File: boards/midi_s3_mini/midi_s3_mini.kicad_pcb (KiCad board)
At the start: 2 copper layers, 90 x 70 mm, 35 parts, among them J1 Power2, J10 PLAY_CUE, J11 JOG, J12 TEMPO, J2 Power1, J3 UART_PI, J4 1BTN_A_TX, J5 1BTN_A_RX, J6 1BTN_B_RX, J7 1BTN_B_TX, J8 LOOP, J9 TRACK_ENC, U1 LOLIN_S3_Mini

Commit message: Design the new power supply system
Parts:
- removed C1, C10, C11, C12, C13, C3, C4, C7, C8, C9: 100n, easyeda2kicad:CAP-TH_L4.2-W3.5-P2.54-D0.5
- removed C2: 1000uF / 35 V, easyeda2kicad:CAP-TH_BD10.0-P5.00-D1.0-FD
- removed C5: 10u / 50 V, easyeda2kicad:CAP-TH_BD5.0-P2.00-D0.8-FD
- removed C6: 22u 50V, easyeda2kicad:CAP-TH_BD5.0-P2.00-D0.5-FD
- removed R1, R3: 1.8k, easyeda2kicad:RES-TH_BD2.4-L6.3-P10.30-D0.6
- removed R2, R4: 3.3k, easyeda2kicad:RES-TH_BD2.2-L6.5-P10.50-D0.6
- removed R5: 10k, easyeda2kicad:RES-TH_BD2.5-L6.5-P10.50-D0.6
- moved J11 75.4 mm to (84.9, 85.6), turned to 180 degrees
- moved J12 74.5 mm to (99.6, 85.7), turned to 0 degrees
- moved J8 74.5 mm to (33.7, 85.8), turned to 0 degrees
- moved J3 70.9 mm to (22.2, 56.9), turned to -90 degrees
- moved U1 35.1 mm to (47.9, 24.3), turned to 0 degrees
- moved J1 13.5 mm to (23.4, 44.7)
- moved J2 13.5 mm to (23.4, 35.0)
- moved J10 7.75 mm to (52.4, 85.7)
- moved J9 1.77 mm to (69.2, 85.6)
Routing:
- net +5V: track 193.9 -> 0.00 mm, vias 2 -> 0
- net +3.3V: track 58.4 -> 0.00 mm, vias 3 -> 0
- net /1BTNA_TX: track 52.5 -> 0.00 mm, vias 1 -> 0
- net /1BTNB_TX: track 45.6 -> 0.00 mm, vias 1 -> 0
- net /JOG1: track 44.6 -> 0.00 mm
- net /1BTNA_RX: track 40.3 -> 0.00 mm, vias 1 -> 0
- net /JOG2: track 39.0 -> 0.00 mm
- net /1BTNB_RX: track 35.2 -> 0.00 mm, vias 1 -> 0
- net /UART_RX_FROM_PI: track 33.5 -> 0.00 mm
- net /BTN_PLAY: track 31.8 -> 0.00 mm
- net /LOOP_END_BTN: track 30.2 -> 0.00 mm, vias 1 -> 0
- net /LED_CUE: track 28.8 -> 0.00 mm
- net /BTN_CUE: track 28.6 -> 0.00 mm
- net /LED_PLAY: track 28.4 -> 0.00 mm
- net /ENC_SW: track 27.3 -> 0.00 mm
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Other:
- board text added: "vvv USB-C side vvv"

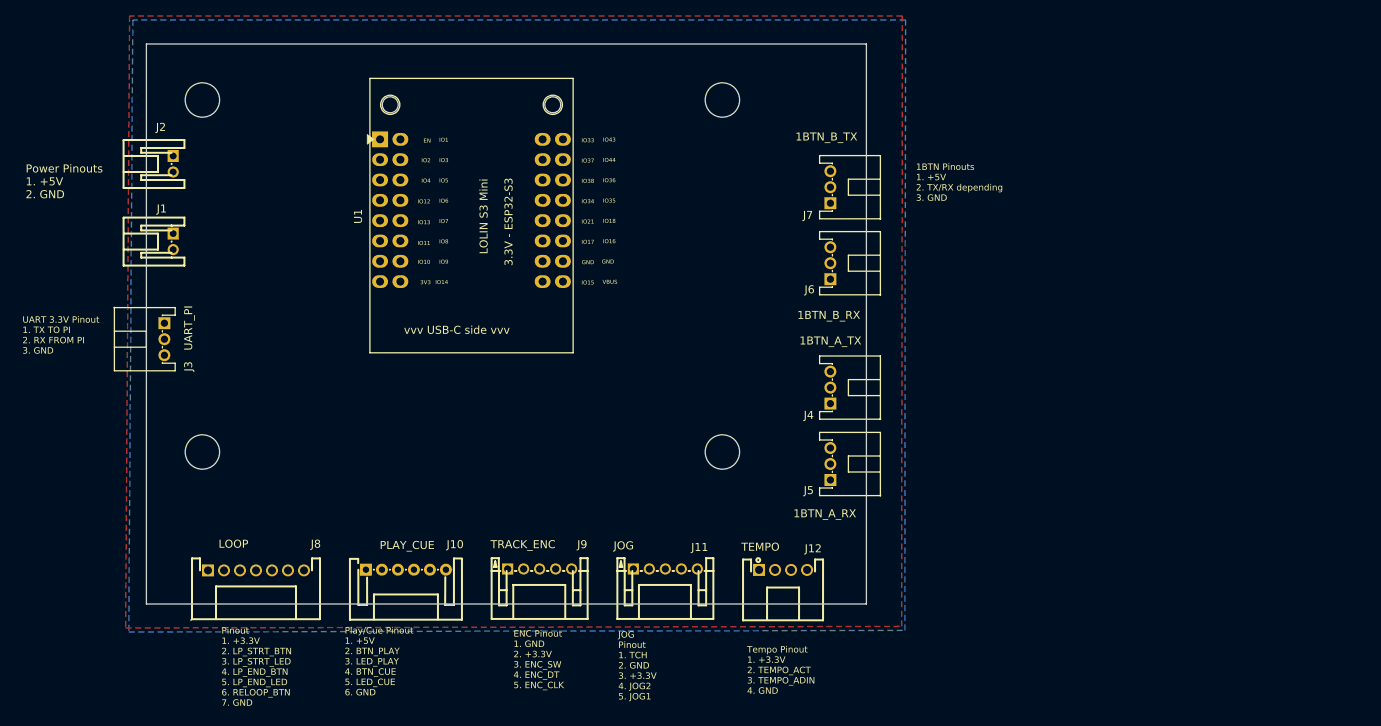
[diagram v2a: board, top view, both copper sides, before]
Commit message: Finish the ESD and power system for the V2 midi S3
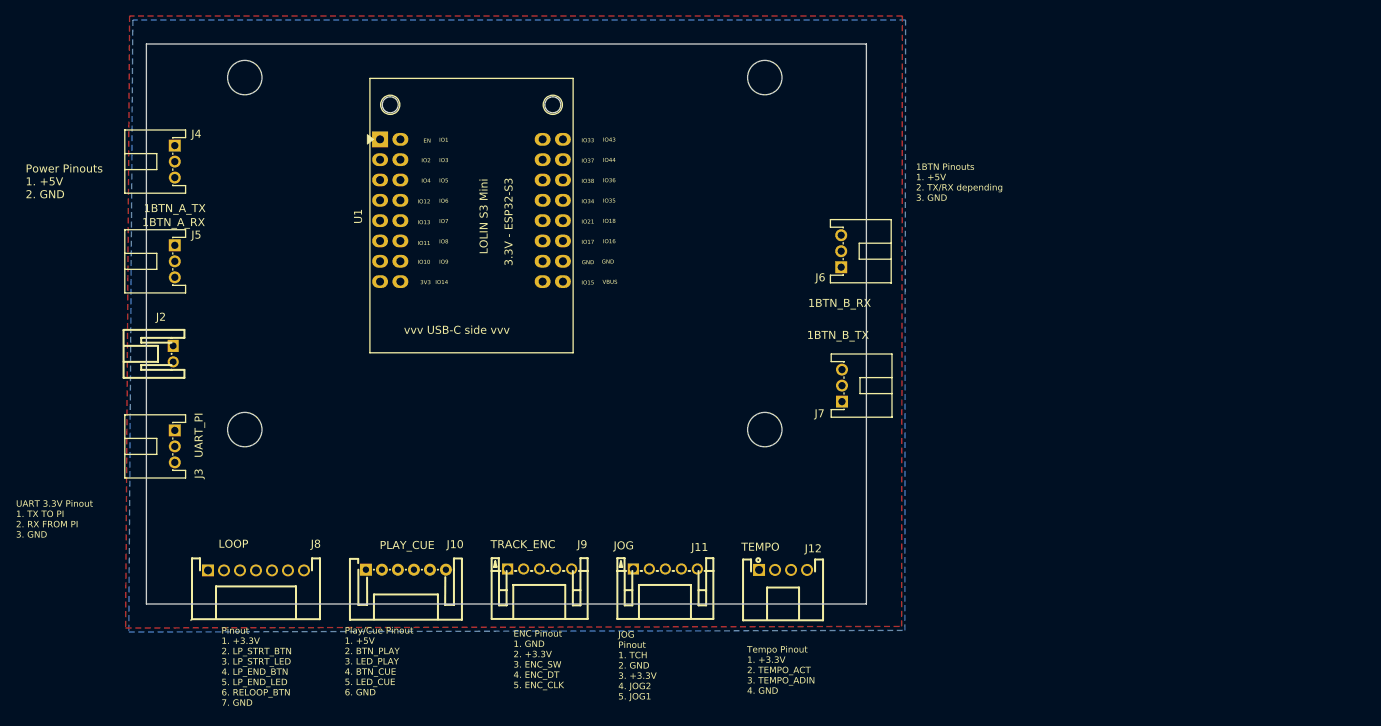
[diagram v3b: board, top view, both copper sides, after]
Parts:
- removed J1: Power2, easyeda2kicad:CONN-TH_S2B-PH-K-S-LF-SN
- moved J4 86.7 mm to (23.6, 34.7), turned to -90 degrees
- moved J5 85.8 mm to (23.6, 47.2), turned to -90 degrees
- moved J7 24.8 mm to (107.0, 62.7)
- moved J2 23.7 mm to (23.4, 58.7)
- moved J3 13.5 mm to (23.6, 70.3)
- moved H1 5.99 mm to (97.3, 24.2)
- moved H2 5.99 mm to (32.3, 24.2)
- moved H3 5.99 mm to (97.3, 68.2)
- moved H4 5.99 mm to (32.3, 68.2)
- moved J6 2.02 mm to (106.8, 45.9)

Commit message: Last tiny net fixes before PCB traces
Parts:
- removed J11: JOG, easyeda2kicad:CONN-TH_S5B-PH-K-S-LF-SN
- removed the J2 at (23.4, 58.7)
- removed the J3 at (23.6, 70.3)
- added C1: 100n, easyeda2kicad:C0402, F.Cu at (139.5, 44.7)
- added C10: 100n, easyeda2kicad:C0402, F.Cu at (142.4, 51.2)
- added C14: 1000uF / 35 V, easyeda2kicad:CAP-TH_BD10.0-P5.00-D1.0-FD, F.Cu at (148.3, 77.7)
- added C15: 100n, easyeda2kicad:C0402, F.Cu at (166.4, 78.1)
- added C16: 22uF 25V, easyeda2kicad:C0805, F.Cu at (157.3, 58.7)
- added C17: 22uF 25V, easyeda2kicad:C0805, F.Cu at (157.3, 61.7)
- added C18: 22uF 25V, easyeda2kicad:C0805, F.Cu at (157.3, 64.6)
- added C19: 100n, easyeda2kicad:C0402, F.Cu at (166.4, 80.2)
- added C2: 100n, easyeda2kicad:C0402, F.Cu at (139.5, 46.9)
- added C20: 4.7uF ±10% 25V, easyeda2kicad:C0805, F.Cu at (157.3, 67.6)
- added C21: 100n, easyeda2kicad:C0402, F.Cu at (166.4, 82.4)
- added C22: 100n, easyeda2kicad:C0402, F.Cu at (142.4, 53.3)
- added C3: 10nF ±10% 50V, easyeda2kicad:C0402, F.Cu at (139.5, 49.0)
- added C4: 100n, easyeda2kicad:C0402, F.Cu at (139.5, 51.2)
- added C5: 100n, easyeda2kicad:C0402, F.Cu at (139.5, 53.3)
- added C7: 100n, easyeda2kicad:C0402, F.Cu at (142.4, 44.7)
- added C8: 100n, easyeda2kicad:C0402, F.Cu at (142.4, 46.9)
- added C9: 100n, easyeda2kicad:C0402, F.Cu at (142.4, 49.0)
- added C_LDO_in1: 1uF ±10% 50V, easyeda2kicad:C0603, F.Cu at (140.1, 85.8)
- added C_LDO_out1: 2.2uF (225) ±20% 50V, easyeda2kicad:C0805, F.Cu at (157.3, 70.5)
- added D1: P6SMB6.8CA, easyeda2kicad:SMB_L4.6-W3.6-LS5.3-BI, F.Cu at (162.4, 74.5)
- added D2: B5819W_C8598, easyeda2kicad:SOD-123_L2.7-W1.6-LS3.7-RD-1, F.Cu at (145.5, 84.8)
- added D_PERI1: SS14, easyeda2kicad:SMA_L4.2-W2.6-LS5.0-RD_1, F.Cu at (161.7, 78.9)
- added D_S1: SS14, easyeda2kicad:SMA_L4.2-W2.6-LS5.0-RD_1, F.Cu at (161.7, 82.8)
- added J10: JOG, easyeda2kicad:CONN-TH_S5B-PH-K-S-LF-SN, F.Cu at (84.9, 85.4)
- added J13: PowerIn, TerminalBlock_Altech:Altech_AK300_1x02_P5.00mm_45-Degree, F.Cu at (24.2, 56.1)
- added J14: TEST_5V, Connector_PinHeader_2.54mm:PinHeader_1x01_P2.54mm_Vertical, F.Cu at (140.4, 59.5)
- added J15: GND_IN, Connector_PinHeader_2.54mm:PinHeader_1x01_P2.54mm_Vertical, F.Cu at (140.4, 64.1)
- added J16: TEST_3V3_S3, Connector_PinHeader_2.54mm:PinHeader_1x01_P2.54mm_Vertical, F.Cu at (140.4, 68.7)
- added J17: TEST_3V3_PERI, Connector_PinHeader_2.54mm:PinHeader_1x01_P2.54mm_Vertical, F.Cu at (140.4, 73.3)
- added J18: GND_PERI, Connector_PinHeader_2.54mm:PinHeader_1x01_P2.54mm_Vertical, F.Cu at (140.4, 77.9)
- added J5: UART_PI, easyeda2kicad:CONN-TH_4P-P2.00_S4B-PH-K-S-LF-SN, F.Cu at (23.9, 75.0)
- added JP1: Power3V3_from_USB, Connector_PinHeader_2.54mm:PinHeader_1x02_P2.54mm_Vertical, F.Cu at (165.1, 59.5)
- added LED_3V3_PERI1: Yellow, easyeda2kicad:LED0805-R-RD, F.Cu at (165.7, 66.0)
- added LED_3V3_S1: Green, easyeda2kicad:LED0805-R-RD, F.Cu at (165.7, 69.3)
- added LED_5V1: Red, easyeda2kicad:LED0805-RD, F.Cu at (151.0, 84.9)
- added Q1: AO3401A, easyeda2kicad:SOT-23_L2.9-W1.3-P1.90-LS2.4-BR, F.Cu at (140.2, 82.3)
- added R1: 1KΩ ±1%, easyeda2kicad:R0402, F.Cu at (139.6, 29.7)
- added R10: 1KΩ ±1%, easyeda2kicad:R0402, F.Cu at (139.6, 42.6)
- added R11: 1KΩ ±1%, easyeda2kicad:R0402, F.Cu at (142.6, 29.7)
- added R12: 1KΩ ±1%, easyeda2kicad:R0402, F.Cu at (142.6, 31.8)
- added R13: 1KΩ ±1%, easyeda2kicad:R0402, F.Cu at (142.6, 34.0)
- added R14: 1KΩ ±1%, easyeda2kicad:R0402, F.Cu at (142.6, 36.1)
- added R15: 1KΩ ±1%, easyeda2kicad:R0402, F.Cu at (142.6, 38.3)
- added R16: 1KΩ ±1%, easyeda2kicad:R0402, F.Cu at (142.6, 40.4)
- added R18: 1KΩ ±1%, easyeda2kicad:R0402, F.Cu at (142.6, 42.6)
- added R19: 1KΩ ±1%, easyeda2kicad:R0402, F.Cu at (145.7, 29.7)
- added R2: 1KΩ ±1%, easyeda2kicad:R0402, F.Cu at (139.6, 31.8)
- added R20: 1KΩ ±1%, easyeda2kicad:R0402, F.Cu at (145.7, 31.8)
- added R21: 1KΩ ±1%, easyeda2kicad:R0402, F.Cu at (145.7, 34.0)
- added R22: 1KΩ ±1%, easyeda2kicad:R0402, F.Cu at (145.7, 36.1)
- added R23: 1KΩ ±1%, easyeda2kicad:R0402, F.Cu at (145.7, 38.3)
- added R24: 1KΩ ±1%, easyeda2kicad:R0402, F.Cu at (145.7, 40.4)
- added R25: 1KΩ ±1%, easyeda2kicad:R0402, F.Cu at (145.7, 42.6)
- added R26: 1KΩ ±1%, easyeda2kicad:R0402, F.Cu at (148.7, 29.7)
- added R3: 22KΩ ±1%, easyeda2kicad:R0402, F.Cu at (161.3, 58.3)
- added R30: 3.3KΩ ±1%, easyeda2kicad:R0402, F.Cu at (161.3, 62.6)
- added R31: 100KΩ ±1%, easyeda2kicad:R0603, F.Cu at (160.4, 85.9)
- added R34: 1Ω ±1%, easyeda2kicad:R0402, F.Cu at (161.3, 64.8)
- added R35: 470Ω ±1%, easyeda2kicad:R0402, F.Cu at (161.3, 66.9)
- added R36: 1.5KΩ ±1%, easyeda2kicad:R0402, F.Cu at (161.3, 69.1)
- added R37: 1.8KΩ ±1%, easyeda2kicad:R0603, F.Cu at (165.4, 38.9)
- added R38: 3.3KΩ ±1%, easyeda2kicad:R0402, F.Cu at (148.7, 31.8)
- added R39: 3.3KΩ ±1%, easyeda2kicad:R0402, F.Cu at (148.7, 34.0)
- added R4: 47KΩ ±1%, easyeda2kicad:R0402, F.Cu at (161.3, 60.5)
- added R40: 1.8KΩ ±1%, easyeda2kicad:R0603, F.Cu at (165.4, 41.3)
- added R5: 10KΩ ±1%, easyeda2kicad:R0402, F.Cu at (139.6, 34.0)
- added R7: 1KΩ ±1%, easyeda2kicad:R0402, F.Cu at (139.6, 36.1)
- added R8: 1KΩ ±1%, easyeda2kicad:R0402, F.Cu at (139.6, 38.3)
- added R9: 1KΩ ±1%, easyeda2kicad:R0402, F.Cu at (139.6, 40.4)
- added TP1: VBUS_S3, TestPoint:TestPoint_Pad_D2.5mm, F.Cu at (163.7, 30.9)
- added TP2: VIN_5V, TestPoint:TestPoint_Pad_D2.5mm, F.Cu at (156.2, 74.3)
- added TP3: LDO_OUT, TestPoint:TestPoint_Pad_D2.5mm, F.Cu at (156.2, 78.9)
- added TVS1: SRV05-4, easyeda2kicad:SOT-23-6_L2.9-W1.6-P0.95-LS2.8-BL, F.Cu at (152.7, 48.7)
- added TVS2: SRV05-4, easyeda2kicad:SOT-23-6_L2.9-W1.6-P0.95-LS2.8-BL, F.Cu at (152.7, 53.0)
- added TVS3: SRV05-4, easyeda2kicad:SOT-23-6_L2.9-W1.6-P0.95-LS2.8-BL, F.Cu at (157.3, 48.7)
- added TVS4: SRV05-4, easyeda2kicad:SOT-23-6_L2.9-W1.6-P0.95-LS2.8-BL, F.Cu at (157.3, 53.0)
- added TVS5: SRV05-4, easyeda2kicad:SOT-23-6_L2.9-W1.6-P0.95-LS2.8-BL, F.Cu at (161.8, 48.7)
- added TVS6: SRV05-4, easyeda2kicad:SOT-23-6_L2.9-W1.6-P0.95-LS2.8-BL, F.Cu at (161.8, 53.0)
- added TVS7: SRV05-4, easyeda2kicad:SOT-23-6_L2.9-W1.6-P0.95-LS2.8-BL, F.Cu at (166.4, 48.7)
- added TVS8: SRV05-4, easyeda2kicad:SOT-23-6_L2.9-W1.6-P0.95-LS2.8-BL, F.Cu at (166.4, 53.0)
- added U2: SPX3819M5-L/TR, easyeda2kicad:SOT-23-5_L3.0-W1.7-P0.95-LS2.8-TL, F.Cu at (156.2, 83.5)
- J1: renamed from J4; value 1BTN_A_TX -> OneButtonA_TX
- J2: renamed from J5; value 1BTN_A_RX -> OneButtonA_RX
- J3: renamed from J6; value 1BTN_B_RX -> OneButtonB_RX
- J4: renamed from J7; value 1BTN_B_TX -> OneButtonB_TX
- moved H1 7.70 mm to (105.0, 24.2)
- moved H2 7.70 mm to (40.0, 24.2)
- moved H3 7.70 mm to (105.0, 68.2)
- moved H4 7.70 mm to (40.0, 68.2)
- moved J4 7.23 mm to (106.2, 55.5)
- moved J3 7.23 mm to (106.2, 38.7)
- renumbered J9 to J6, J8 to J7, J10 to J8, J12 to J9
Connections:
- J1 pad 2: /1BTNA_TX -> /RAW_1BTNA_TX
- J4 pad 2: /1BTNB_TX -> /RAW_1BTNB_TX
- J6 pad 3: /ENC_SW -> /RAW_ENC_SW
- J6 pad 4: /ENC_DT -> /RAW_ENC_DT
- J6 pad 5: /ENC_CLK -> /RAW_ENC_CLK
- J7 pad 2: /LOOP_START_BTN -> /RAW_LOOP_START_BTN
- J7 pad 3: /LOOP_START_LED -> /RAW_LOOP_START_LED
- J7 pad 4: /LOOP_END_BTN -> /RAW_LOOP_END_BTN
- J7 pad 5: /LOOP_END_LED -> /RAW_LOOP_END_LED
- J7 pad 6: /RELOOP_BTN -> /RAW_RELOOP_BTN
- J8 pad 2: /BTN_PLAY -> /RAW_BTN_PLAY
- J8 pad 3: /LED_PLAY -> /RAW_LED_PLAY
- J8 pad 4: /BTN_CUE -> /RAW_BTN_CUE
- J8 pad 5: /LED_CUE -> /RAW_LED_CUE
- J9 pad 2: /TEMPO_ADCT -> /RAW_TEMPO_ADCT
- J9 pad 3: /TEMPO_ADIN -> /RAW_TEMPO_ADIN
- U1 pad 16: /JOG_TCH -> unconnected-(U1-IO14-Pad16)
- U1 pad 32: +5V -> S3_VBUS_5V
- U1 pad 6: unconnected-(U1-IO11/MOSI-Pad6) -> /JOG_TCH
- U1 pad 8: +3.3V -> S3_3.3V
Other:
- board text added: "UART 3.3V Pinout 1. GND 2. TX TO PI 3. RX FROM PI 4. GND"
- board text removed: "UART 3.3V Pinout 1. TX TO PI 2. RX FROM PI 3. GND"

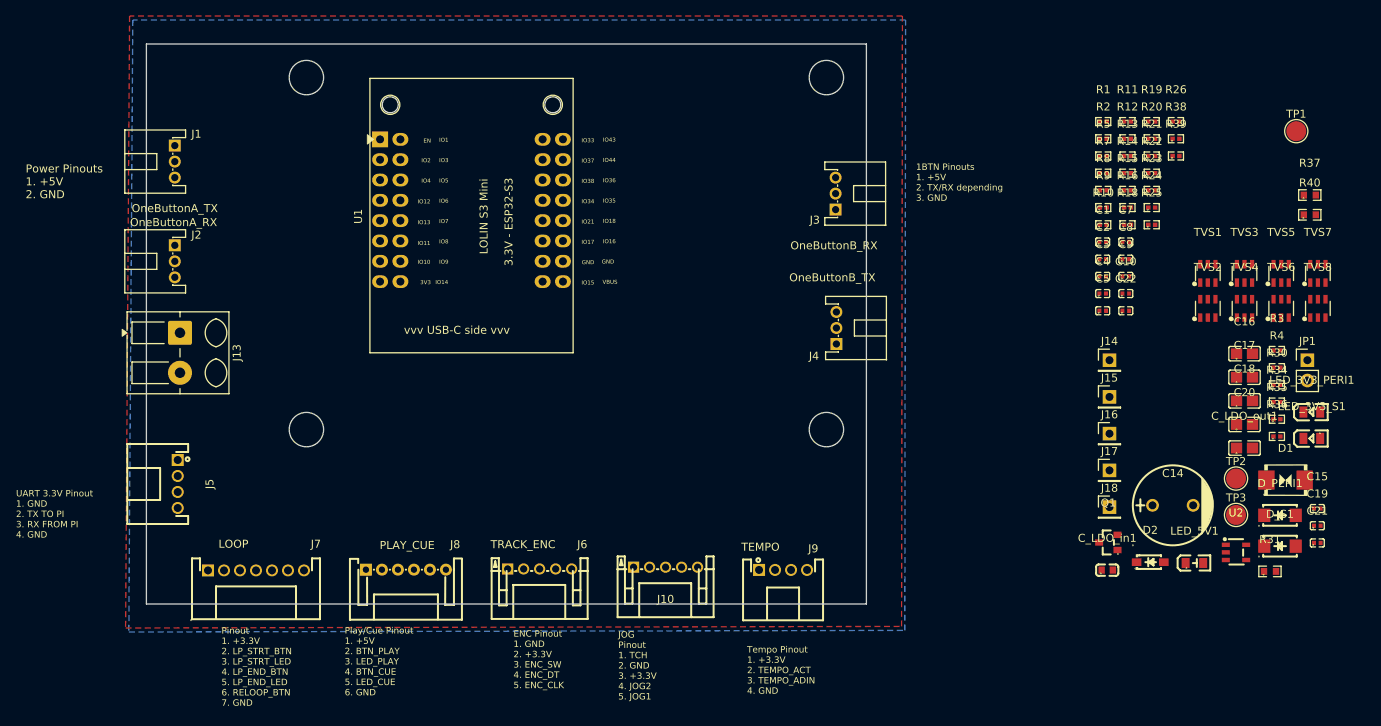
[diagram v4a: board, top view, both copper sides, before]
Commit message: Lay down PCB with no GND plane breaks
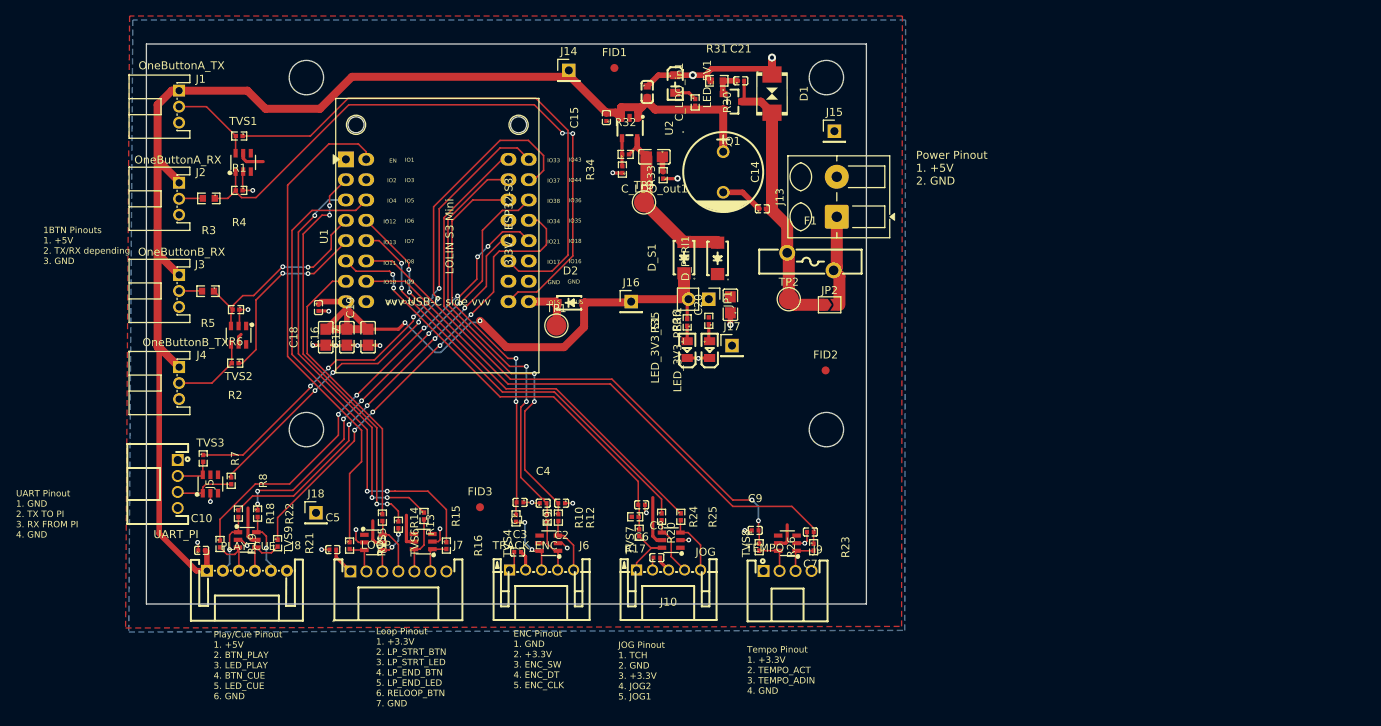
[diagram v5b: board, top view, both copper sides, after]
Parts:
- added C21: 100n, easyeda2kicad:C0402, F.Cu at (94.3, 24.6)
- added F1: MF-R250, easyeda2kicad:FUSE-TH_L12.8-W3.0-P5.80-D1.2-S2.20, F.Cu at (103.0, 47.2)
- added FID1: Fiducial, Fiducial:Fiducial_1mm_Mask2mm, F.Cu at (78.5, 23.0)
- added FID2: Fiducial, Fiducial:Fiducial_1mm_Mask2mm, F.Cu at (104.9, 60.8)
- added FID3: Fiducial, Fiducial:Fiducial_1mm_Mask2mm, F.Cu at (61.7, 77.9)
- added JP2: SolderJumper_2_Open, Jumper:SolderJumper-2_P1.3mm_Open_TrianglePad1.0x1.5mm, F.Cu at (105.4, 52.6)
- added TVS2: SRV05-4, easyeda2kicad:SOT-23-6_L2.9-W1.6-P0.95-LS2.8-BL, F.Cu at (31.5, 56.4)
- moved R5 138.1 mm to (27.7, 50.9), turned to 180 degrees
- moved R3 137.6 mm to (27.8, 39.3), turned to 180 degrees
- moved TVS9 136.9 mm to (32.6, 82.0), turned to -90 degrees
- moved R19 127.9 mm to (29.2, 82.5), turned to -90 degrees
- moved C19 127.8 mm to (41.5, 53.0), turned to -90 degrees
- moved TVS3 126.6 mm to (28.0, 75.0)
- moved TVS1 121.4 mm to (32.1, 34.8)
- moved C10 119.9 mm to (26.9, 83.3)
- moved R22 119.6 mm to (33.9, 78.7), turned to -90 degrees
- moved R21 119.5 mm to (36.4, 82.4), turned to -90 degrees
- moved R6 119.1 mm to (31.2, 53.2), turned to 180 degrees
- moved TVS6 118.3 mm to (48.4, 82.3), turned to -90 degrees
- moved R7 118.0 mm to (27.1, 71.8), turned to -90 degrees
- moved R4 117.3 mm to (31.6, 38.3), turned to 180 degrees
- moved R18 116.9 mm to (31.5, 78.7), turned to -90 degrees
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- renumbered C21 to C13, C22 to C6, R5 to R17, R37 to R3, R4 to R32, R34 to R33, R3 to R34, R38 to R4, R40 to R5, R39 to R6, TVS2 to TVS3, TVS3 to TVS4, TVS4 to TVS5, TVS5 to TVS6, TVS6 to TVS7, TVS7 to TVS8, TVS8 to TVS9
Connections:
- D2 pad 2: +3.3V -> S3_3.3V
- J13 pad 1: /Power/VIN_5V -> Net-(J13-Pin_1)
- TVS1 pad 3: /1BTNB_RX -> unconnected-(TVS1-Pad3)
- TVS1 pad 4: /RAW_1BTNA_TX -> unconnected-(TVS1-Pad4)
- TVS1 pad 6: /RAW_1BTNB_TX -> /RAW_1BTNA_TX
- TVS3 pad 1: unconnected-(TVS2-Pad1) -> /RAW_UART_RX_FROM_PI
- TVS3 pad 4: /RAW_UART_TX_TO_PI -> unconnected-(TVS3-Pad4)
- TVS3 pad 6: /RAW_UART_RX_FROM_PI -> /RAW_UART_TX_TO_PI
- TVS4 pad 1: /RAW_ENC_SW -> /RAW_ENC_DT
- TVS4 pad 6: /RAW_ENC_DT -> /RAW_ENC_SW
- TVS5 pad 1: /RAW_LOOP_END_BTN -> /RAW_RELOOP_BTN
- TVS5 pad 4: /RAW_RELOOP_BTN -> unconnected-(TVS5-Pad4)
- TVS5 pad 6: /RAW_LOOP_START_BTN -> /RAW_LOOP_END_LED
- TVS6 pad 3: unconnected-(TVS5-Pad3) (its old number) -> /RAW_LOOP_START_BTN
- TVS6 pad 6: /RAW_LOOP_END_LED -> /RAW_LOOP_END_BTN
- TVS7 pad 1: /RAW_JOG1 -> unconnected-(TVS7-Pad1)
- TVS7 pad 3: unconnected-(TVS6-Pad3) -> /RAW_JOG1
- TVS8 pad 1: unconnected-(TVS7-Pad1) -> /RAW_TEMPO_ADIN
- TVS8 pad 4: /RAW_TEMPO_ADCT -> unconnected-(TVS8-Pad4)
- TVS8 pad 6: /RAW_TEMPO_ADIN -> /RAW_TEMPO_ADCT
- TVS9 pad 1: /RAW_LED_CUE -> /RAW_BTN_PLAY
- TVS9 pad 3: /RAW_BTN_CUE -> /RAW_LED_PLAY
- TVS9 pad 4: /RAW_LED_PLAY -> /RAW_BTN_CUE
- TVS9 pad 6: /RAW_BTN_PLAY -> /RAW_LED_CUE
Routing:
- net +5V: track 0.00 -> 161.2 mm
- net /1BTNA_RX: track 0.00 -> 80.2 mm, vias 0 -> 2
- net S3_3.3V: track 0.00 -> 75.7 mm, vias 0 -> 2
- net GND: track 0.00 -> 72.8 mm, vias 0 -> 26
- net /TEMPO_ADIN: track 0.00 -> 70.7 mm
- net /UART_RX_FROM_PI: track 0.00 -> 69.5 mm, vias 0 -> 4
- net /1BTNA_TX: track 0.00 -> 68.7 mm
- net /TEMPO_ADCT: track 0.00 -> 66.4 mm, vias 0 -> 2
- net /UART_TX_TO_PI: track 0.00 -> 63.8 mm, vias 0 -> 4
- net /LOOP_START_BTN: track 0.00 -> 62.5 mm
- net /RELOOP_BTN: track 0.00 -> 62.3 mm, vias 0 -> 2
- net /LED_PLAY: track 0.00 -> 59.8 mm, vias 0 -> 6
- net /BTN_CUE: track 0.00 -> 58.5 mm, vias 0 -> 4
- net /LED_CUE: track 0.00 -> 56.8 mm, vias 0 -> 6
- net /ENC_CLK: track 0.00 -> 56.8 mm, vias 0 -> 2
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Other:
- board text added: "Loop Pinout 1. +3.3V 2. LP_STRT_BTN 3. LP_STRT_LED 4. LP_END_BTN 5. LP_END_LED 6. RELOOP_BTN 7. GND"
- board text added: "Power Pinout 1. +5V 2. GND"
- board text added: "UART Pinout 1. GND 2. TX TO PI 3. RX FROM PI 4. GND"
- board text removed: "Pinout 1. +3.3V 2. LP_STRT_BTN 3. LP_STRT_LED 4. LP_END_BTN 5. LP_END_LED 6. RELOOP_BTN 7. GND"
- board text removed: "Power Pinouts 1. +5V 2. GND"
- board text removed: "UART 3.3V Pinout 1. GND 2. TX TO PI 3. RX FROM PI 4. GND"
